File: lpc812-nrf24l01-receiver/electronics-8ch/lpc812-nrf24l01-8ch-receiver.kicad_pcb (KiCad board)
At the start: 2 copper layers, 21 x 21 mm, 23 parts, among them J1 CH1, J2 CH2, J3 CH3/Rx, J4 CH4/Tx, J5 CH5, J6 CH6, J7 CH7, J8 CH8, SW1 BIND/ISP, U1 MCP1703A-3302_SOT23, U2 LPC812M101JDH20, U3 NRF24L01_E01_ML01, Y1 12 MHz

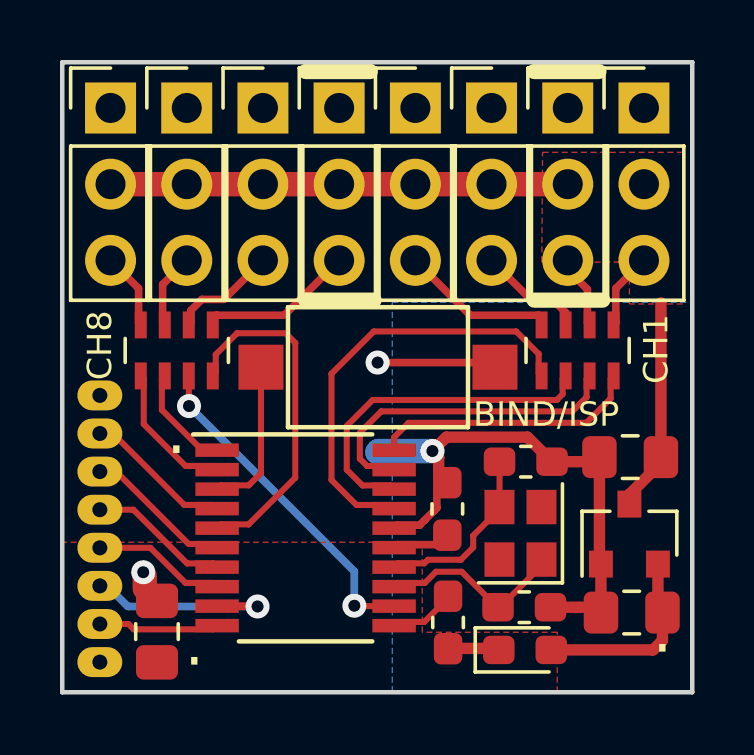
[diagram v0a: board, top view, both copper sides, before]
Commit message: Make PIO10 and PIO11 use as input pins as they are open drain
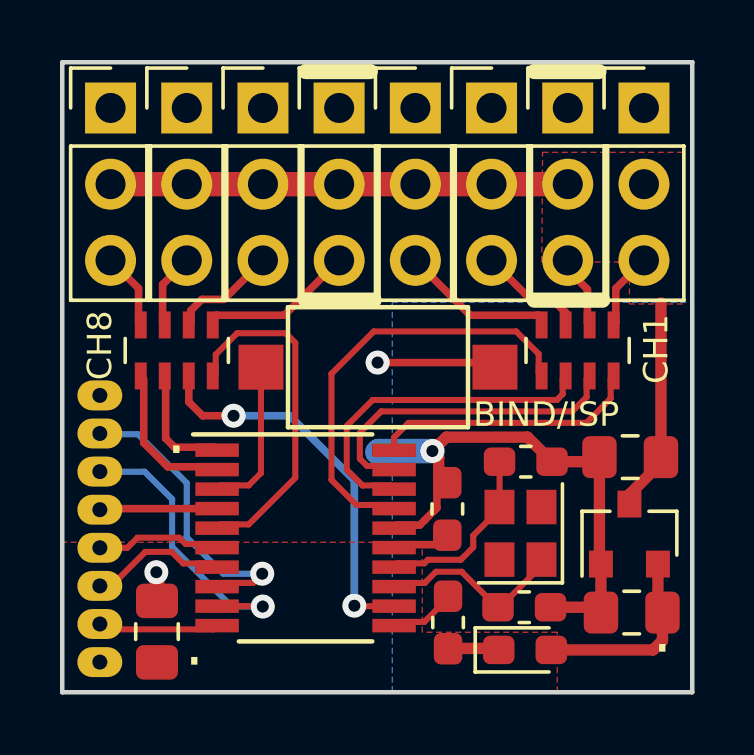
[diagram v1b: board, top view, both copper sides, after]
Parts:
- Y1: value 12 MHz -> 16MHz
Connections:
- U2 pad 4: /IRQ -> /MOSI
- U2 pad 6: /MISO -> /SCK
- U2 pad 7: /MOSI -> /CSN
- U2 pad 8: /SCK -> /IRQ
- U2 pad 9: /CSN -> /MISO
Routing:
- net /IRQ: track 4.95 -> 10.1 mm, vias 0 -> 1
- net /MISO: track 4.96 -> 9.79 mm, vias 0 -> 1
- net /CSN: track 6.90 -> 4.59 mm, vias 1 -> 0
- net /CH6: track 11.5 -> 13.2 mm
- net /MOSI: track 4.70 -> 3.92 mm

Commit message: Tweak layout
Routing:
- net /CH6: track 13.2 -> 12.1 mm
- net /IRQ: track 10.1 -> 9.40 mm
- net /MISO: track 9.79 -> 9.24 mm
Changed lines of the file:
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@@
     (thickness 1.6)
     (drawings 24)
-    (tracks 221)
+    (tracks 216)
     (zones 0)
     (modules 23)
@@
   )
   (setup
-    (last_trace_width 0.254)
+    (last_trace_width 0.2032)
     (user_trace_width 0.254)
     (user_trace_width 0.381)
@@
   (segment (start 119.2882 81.8798) (end 119.253 81.915) (width 0.2032) (layer F.Cu) (net 21) (status 30))
   (segment (start 123.161 81.8798) (end 119.2882 81.8798) (width 0.254) (layer F.Cu) (net 21) (status 30))
-  (segment (start 124.669982 85.1298) (end 124.68352 85.143338) (width 0.2032) (layer F.Cu) (net 22))
-  (segment (start 123.161 85.1298) (end 124.669982 85.1298) (width 0.2032) (layer F.Cu) (net 22) (status 10))
-  (via (at 124.68352 85.143338) (size 0.8) (drill 0.4) (layers F.Cu B.Cu) (net 22))
-  (segment (start 123.652278 85.143338) (end 124.68352 85.143338) (width 0.2032) (layer B.Cu) (net 22))
-  (segment (start 120.74398 80.64754) (end 121.66346 81.56702) (width 0.2032) (layer B.Cu) (net 22))
-  (segment (start 119.27332 80.7847) (end 119.41048 80.64754) (width 0.2032) (layer B.Cu) (net 22))
-  (segment (start 121.66346 83.15452) (end 123.652278 85.143338) (width 0.2032) (layer B.Cu) (net 22))
-  (segment (start 121.66346 81.56702) (end 121.66346 83.15452) (width 0.2032) (layer B.Cu) (net 22))
-  (segment (start 119.41048 80.64754) (end 120.74398 80.64754) (width 0.2032) (layer B.Cu) (net 22))
-  (via (at 124.66574 84.0486) (size 0.8) (drill 0.4) (layers F.Cu B.Cu) (net 23))
-  (segment (start 124.3584 84.35594) (end 124.66574 84.0486) (width 0.2032) (layer F.Cu) (net 23))
-  (segment (start 123.161 84.4798) (end 123.28486 84.35594) (width 0.2032) (layer F.Cu) (net 23) (status 30))
-  (segment (start 123.28486 84.35594) (end 124.3584 84.35594) (width 0.2032) (layer F.Cu) (net 23) (status 10))
-  (segment (start 123.36272 84.0486) (end 124.66574 84.0486) (width 0.2032) (layer B.Cu) (net 23))
-  (segment (start 122.14606 82.83194) (end 123.36272 84.0486) (width 0.2032) (layer B.Cu) (net 23))
-  (segment (start 119.28348 79.4004) (end 120.523 79.4004) (width 0.2032) (layer B.Cu) (net 23) (status 10))
-  (segment (start 122.14606 81.02346) (end 122.14606 82.83194) (width 0.2032) (layer B.Cu) (net 23))
-  (segment (start 120.523 79.4004) (end 122.14606 81.02346) (width 0.2032) (layer B.Cu) (net 23))
+  (via (at 124.714 85.13318) (size 0.8) (drill 0.4) (layers F.Cu B.Cu) (net 22))
+  (segment (start 123.161 85.1298) (end 124.71062 85.1298) (width 0.2032) (layer F.Cu) (net 22) (status 10))
+  (segment (start 124.71062 85.1298) (end 124.714 85.13318) (width 0.2032) (layer F.Cu) (net 22))
+  (segment (start 119.27332 80.7847) (end 121.12752 80.7847) (width 0.2032) (layer B.Cu) (net 22) (status 10))
+  (segment (start 124.70892 85.1281) (end 124.714 85.13318) (width 0.2032) (layer B.Cu) (net 22))
+  (segment (start 124.70892 84.3661) (end 124.70892 85.1281) (width 0.2032) (layer B.Cu) (net 22))
+  (segment (start 121.12752 80.7847) (end 124.70892 84.3661) (width 0.2032) (layer B.Cu) (net 22))
+  (via (at 124.70638 83.29676) (size 0.8) (drill 0.4) (layers F.Cu B.Cu) (net 23))
+  (segment (start 124.70638 83.86262) (end 124.70638 83.29676) (width 0.2032) (layer F.Cu) (net 23))
+  (segment (start 124.0892 84.4798) (end 124.70638 83.86262) (width 0.2032) (layer F.Cu) (net 23))
+  (segment (start 123.161 84.4798) (end 124.0892 84.4798) (width 0.2032) (layer F.Cu) (net 23) (status 10))
+  (segment (start 120.81002 79.4004) (end 124.70638 83.29676) (width 0.2032) (layer B.Cu) (net 23))
+  (segment (start 119.28348 79.4004) (end 120.81002 79.4004) (width 0.2032) (layer B.Cu) (net 23) (status 10))
   (segment (start 123.0392 83.058) (end 123.161 83.1798) (width 0.2032) (layer F.Cu) (net 24) (status 30))
   (segment (start 119.253 83.185) (end 120.17248 83.185) (width 0.2032) (layer F.Cu) (net 24) (status 10))
@@
   (segment (start 122.2184 77.4564) (end 122.2184 78.32466) (width 0.254) (layer F.Cu) (net 32) (status 10))
   (segment (start 122.2184 78.32466) (end 122.67692 78.78318) (width 0.254) (layer F.Cu) (net 32))
-  (segment (start 127.736598 85.1154) (end 127.736598 80.934558) (width 0.254) (layer B.Cu) (net 32))
-  (segment (start 125.58522 78.78318) (end 123.7107 78.78318) (width 0.254) (layer B.Cu) (net 32))
-  (segment (start 127.736598 80.934558) (end 125.58522 78.78318) (width 0.254) (layer B.Cu) (net 32))
+  (segment (start 123.7107 78.8416) (end 123.7107 78.78318) (width 0.254) (layer B.Cu) (net 32))
+  (segment (start 127.736598 85.1154) (end 127.736598 82.867498) (width 0.254) (layer B.Cu) (net 32))
+  (segment (start 127.736598 82.867498) (end 123.7107 78.8416) (width 0.254) (layer B.Cu) (net 32))
   (zone (net 2) (net_name GND) (layer B.Cu) (hatch edge 0.508)
     (connect_pads (clearance 0.254))

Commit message: Tidy up Fab layer
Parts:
- RN1, RN2: value R_Pack04 -> 1k x 4
- Y1: value 16MHz -> 12MHz
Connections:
- Y1 pad 2: Net-(Y1-Pad2) -> (no net)
- Y1 pad 4: Net-(Y1-Pad4) -> (no net)

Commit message: Fix connector label
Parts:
- J2: value CH2 -> CH2/Rx
- J3: value CH3/Rx -> CH3
- J4: value CH4/Tx -> CH4
- J5: value CH5 -> CH5/Tx
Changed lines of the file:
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@@
     (47 F.CrtYd user hide)
     (48 B.Fab user hide)
-    (49 F.Fab user)
+    (49 F.Fab user hide)
   )
   (setup
@@
       (effects (font (size 1 1) (thickness 0.15)))
     )
-    (fp_text value CH2 (at 0 7.41) (layer F.Fab) hide
+    (fp_text value CH2/Rx (at 0 7.41) (layer F.Fab) hide
       (effects (font (size 0.7 0.7) (thickness 0.15)))
     )
@@
       (effects (font (size 1 1) (thickness 0.15)))
     )
-    (fp_text value CH3/Rx (at 0 7.41) (layer F.Fab) hide
+    (fp_text value CH3 (at 0 7.41) (layer F.Fab) hide
       (effects (font (size 0.7 0.7) (thickness 0.15)))
     )
@@
       (effects (font (size 1 1) (thickness 0.15)))
     )
-    (fp_text value CH4/Tx (at 0 7.41) (layer F.Fab) hide
+    (fp_text value CH4 (at 0 7.41) (layer F.Fab) hide
       (effects (font (size 0.7 0.7) (thickness 0.15)))
     )
@@
       (effects (font (size 1 1) (thickness 0.15)))
     )
-    (fp_text value CH5 (at 0 7.41) (layer F.Fab) hide
-      (effects (font (size 0.7 0.7) (thickness 0.15)))
-    )
+    (fp_text value CH5/Tx (at 0 7.41) (layer F.Fab) hide
+      (effects (font (size 0.7 0.7) (thickness 0.15)))
+    )

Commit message: Add Gerber for Rev 1, manufactured 2018-10-14
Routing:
- net VDD: track 22.9 -> 23.6 mm
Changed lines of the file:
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@@
-(kicad_pcb (version 20171130) (host pcbnew 5.0.0-fee4fd1~66~ubuntu18.04.1)
+(kicad_pcb (version 20171130) (host pcbnew 5.0.1-33cea8e~66~ubuntu18.04.1)
   (general
     (thickness 1.6)
     (drawings 24)
-    (tracks 216)
+    (tracks 217)
     (zones 0)
     (modules 23)
@@
     (pad_drill 0.762)
     (pad_to_mask_clearance 0.1016)
+    (solder_mask_min_width 0.25)
     (aux_axis_origin 118 88)
     (visible_elements FFFFFF7F)
     (pcbplotparams
-      (layerselection 0x010fc_ffffffff)
+      (layerselection 0x010f0_ffffffff)
       (usegerberextensions false)
       (usegerberattributes false)
@@
       (outputformat 1)
       (mirror false)
-      (drillshape 1)
+      (drillshape 0)
       (scaleselection 1)
-      (outputdirectory ""))
+      (outputdirectory "gerber/"))
   )
   (net 0 "")
@@
   (segment (start 129.77 71.064) (end 132.31 71.064) (width 0.8128) (layer F.Cu) (net 1) (status 30))
   (segment (start 132.31 71.064) (end 134.85 71.064) (width 0.8128) (layer F.Cu) (net 1) (status 30))
-  (segment (start 137.9564 80.1624) (end 137.9564 75.0226) (width 0.381) (layer F.Cu) (net 1) (status 10))
   (segment (start 137.9564 80.3566) (end 137.9564 80.1624) (width 0.381) (layer F.Cu) (net 1) (status 30))
   (segment (start 136.906 81.7278) (end 136.906 81.407) (width 0.381) (layer F.Cu) (net 1) (status 30))
   (segment (start 136.906 81.407) (end 137.9564 80.3566) (width 0.381) (layer F.Cu) (net 1) (status 30))
+  (segment (start 137.9564 75.0226) (end 138.43 74.549) (width 0.381) (layer F.Cu) (net 1))
+  (segment (start 137.9564 80.1624) (end 137.9564 75.0226) (width 0.381) (layer F.Cu) (net 1))
   (segment (start 129.3114 79.9846) (end 129.3368 79.9592) (width 0.381) (layer B.Cu) (net 2))
   (segment (start 132.424 77.1652) (end 132.2589 77.0001) (width 0.381) (layer F.Cu) (net 2) (status 30))
